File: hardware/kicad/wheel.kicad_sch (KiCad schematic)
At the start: 6 parts, among them J401 Deutsch DTM 3p (sensore), U401 EL817

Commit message: Translate code, hardware and docs to English; bilingual dashboard
- tdm-logic i18n module: every dashboard text in English and Italian,
  chosen by `[display] language` in the profile (English by default, the
  TDM 850 profile keeps Italian); number formatting per language
- Slint fixed labels moved to a `Labels` global filled from the same table;
  `tdm-dash --language en|it`; reference screens regenerated in English with
  Italian check screens
- tdmctl, tdm-dash CLI, simulator scenarios, calibration errors and tools
  print English
- KiCad sheets, WireViz harnesses, perfboard plan and CAD comments in
  English, exports regenerated with the new names
- manual, research, ADRs and READMEs translated; files renamed (docs/manual,
  docs/research, English chapter and ADR names); status markers are now
  [VERIFIED] / [TO VERIFY] / [HYPOTHESIS]

Co-Authored-By: Claude Opus 5.5 <noreply@anthropic.com>
Claude-Session: https://claude.ai/code/session_01G9D4Wshjz9MkaThp4wsrGP
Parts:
- J401: value Deutsch DTM 3p (sensore) -> Deutsch DTM 3p (sensor)
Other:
- note added: "LJ12A3-4-Z/BX inductive NPN normally open: in front of a bolt the output goes to ground. +12V_P → 2.2 kΩ → EL817 LED → sensor output. External 4.7 kΩ pull-up for fast edges. Sensor colours: brown +12 V, blue ground, black signal."
- note added: "Speed sensor"
- note added: "WHEEL → GP2, active low"
- note removed: "LJ12A3-4-Z/BX induttivo NPN normalmente aperto: davanti a un bullone l'uscita va a massa. +12V_P → 2,2 kΩ → LED dell'EL817 → uscita del sensore. Pull-up esterno da 4,7 kΩ per fronti veloci. Colori del sensore: marrone +12 V, blu massa, nero segnale."
- note removed: "Sensore di velocità"
- note removed: "WHEEL → GP2, attivo basso"
- title: Sensore ruota (LJ12A3) -> Wheel sensor (LJ12A3)
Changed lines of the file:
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@@
 	(paper "A4")
 	(title_block
-		(title "Sensore ruota (LJ12A3)")
+		(title "Wheel sensor (LJ12A3)")
 		(date "2026-10-21")
 		(rev "0.1")
 		(company "tdm-dash · CERN-OHL-P-2.0")
-		(comment 1 "Foglio 4 di 8")
-		(comment 2 "Generato da hardware/kicad/generate.py: non modificare a mano")
+		(comment 1 "Sheet 4 of 8")
+		(comment 2 "Generated by hardware/kicad/generate.py: do not edit by hand")
 	)
 	(symbol
@@
 			)
 		)
-		(property "Value" "Deutsch DTM 3p (sensore)"
+		(property "Value" "Deutsch DTM 3p (sensor)"
 			(at 30.48 71.12 0)
 			(effects
@@
 		)
 	)
-	(text "Sensore di velocità"
+	(text "Speed sensor"
 		(exclude_from_sim no)
 		(at 10.16 12.7 0)
@@
 		)
 	)
-	(text "LJ12A3-4-Z/BX induttivo NPN normalmente aperto: davanti a un bullone l'uscita va a massa.\n+12V_P → 2,2 kΩ → LED dell'EL817 → uscita del sensore. Pull-up esterno da 4,7 kΩ per fronti veloci.\nColori del sensore: marrone +12 V, blu massa, nero segnale."
+	(text "LJ12A3-4-Z/BX inductive NPN normally open: in front of a bolt the output goes to ground.\n+12V_P → 2.2 kΩ → EL817 LED → sensor output. External 4.7 kΩ pull-up for fast edges.\nSensor colours: brown +12 V, blue ground, black signal."
 		(exclude_from_sim no)
 		(at 10.16 17.78 0)
@@
 		)
 	)
-	(text "WHEEL → GP2, attivo basso"
+	(text "WHEEL → GP2, active low"
 		(exclude_from_sim no)
 		(at 167.64 81.28 0)

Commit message: English README, ADR 0012, CLAUDE.md rules, banner; consistent spelling
- README and docs/assets in English, banner tagline "Open-source digital
  instrument cluster" and regenerated banner
- ADR 0012: English repository, bilingual dashboard
- CLAUDE.md: English everywhere, dashboard texts in both languages through
  tdm-logic i18n, new status markers
- American spelling across docs, harness labels and schematic notes;
  ADR 0007 renamed to 0007-licenses; exports and screens regenerated

Co-Authored-By: Claude Opus 5.5 <noreply@anthropic.com>
Claude-Session: https://claude.ai/code/session_01G9D4Wshjz9MkaThp4wsrGP
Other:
- note added: "LJ12A3-4-Z/BX inductive NPN normally open: in front of a bolt the output goes to ground. +12V_P → 2.2 kΩ → EL817 LED → sensor output. External 4.7 kΩ pull-up for fast edges. Sensor colors: brown +12 V, blue ground, black signal."
- note removed: "LJ12A3-4-Z/BX inductive NPN normally open: in front of a bolt the output goes to ground. +12V_P → 2.2 kΩ → EL817 LED → sensor output. External 4.7 kΩ pull-up for fast edges. Sensor colours: brown +12 V, blue ground, black signal."
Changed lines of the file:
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@@
 		)
 	)
-	(text "LJ12A3-4-Z/BX inductive NPN normally open: in front of a bolt the output goes to ground.\n+12V_P → 2.2 kΩ → EL817 LED → sensor output. External 4.7 kΩ pull-up for fast edges.\nSensor colours: brown +12 V, blue ground, black signal."
+	(text "LJ12A3-4-Z/BX inductive NPN normally open: in front of a bolt the output goes to ground.\n+12V_P → 2.2 kΩ → EL817 LED → sensor output. External 4.7 kΩ pull-up for fast edges.\nSensor colors: brown +12 V, blue ground, black signal."
 		(exclude_from_sim no)
 		(at 10.16 17.78 0)

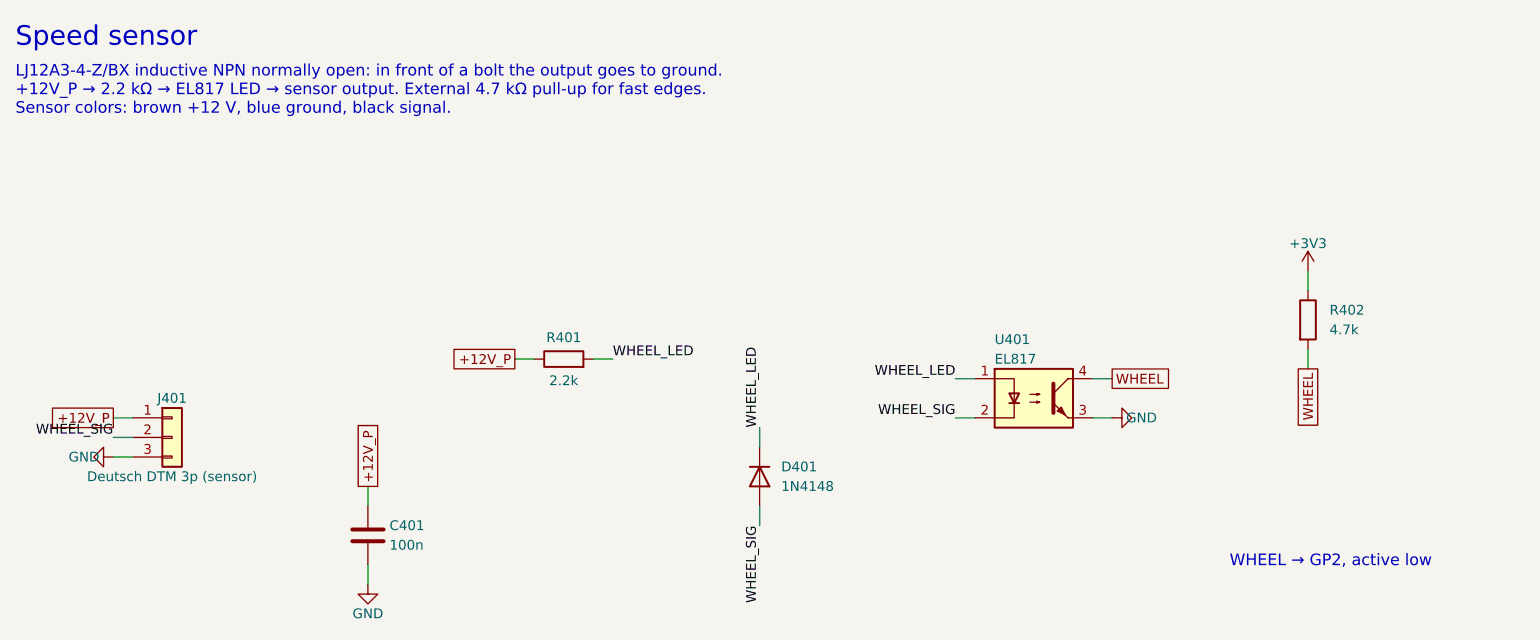
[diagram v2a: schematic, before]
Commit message: Schematic: drawn wires, block diagram, new title block
The sheets were a netlist in disguise: every pin ended in a short stub and
a label, so the circuits had to be pieced together by name, labels
overlapped, two sheets fell off the index page and the title block was
KiCad's default. The generator now draws the schematic:

- hardware/kicad/schgen: placement on the 50 mil grid, orthogonal wires,
  junctions, hierarchical ports, module and connector symbols with named
  pins; the drawing is normalised the way KiCad 9 reads it and checked
  against the declared netlist (no wire may connect anything else)
- hardware/kicad/sheets: one module per sheet, laid out left to right
  from the bike to the Pico; the root sheet is a block diagram whose
  wires are the signals between sheets
- tdm-dash.kicad_wks: frame and title block of the project
- symbols copied from KiCad 9.0.9 (vendor_symbols.py): the generator no
  longer needs KiCad installed
- export.sh: ERC, tools/check_netlist.py (KiCad's netlist is the declared
  one), check_pinmap.py, PDF and SVG on white, tools/check_svg_layout.py
  (no text over another text, a wire, the frame or the title block)

The circuit is unchanged: KiCad's netlist of the old and new schematic
has the same 56 nets (FRAM pins now follow the breakout header, R603/R604
pins swapped).

Co-Authored-By: Claude Opus 5.5 <noreply@anthropic.com>
Claude-Session: https://claude.ai/code/session_01G9D4Wshjz9MkaThp4wsrGP
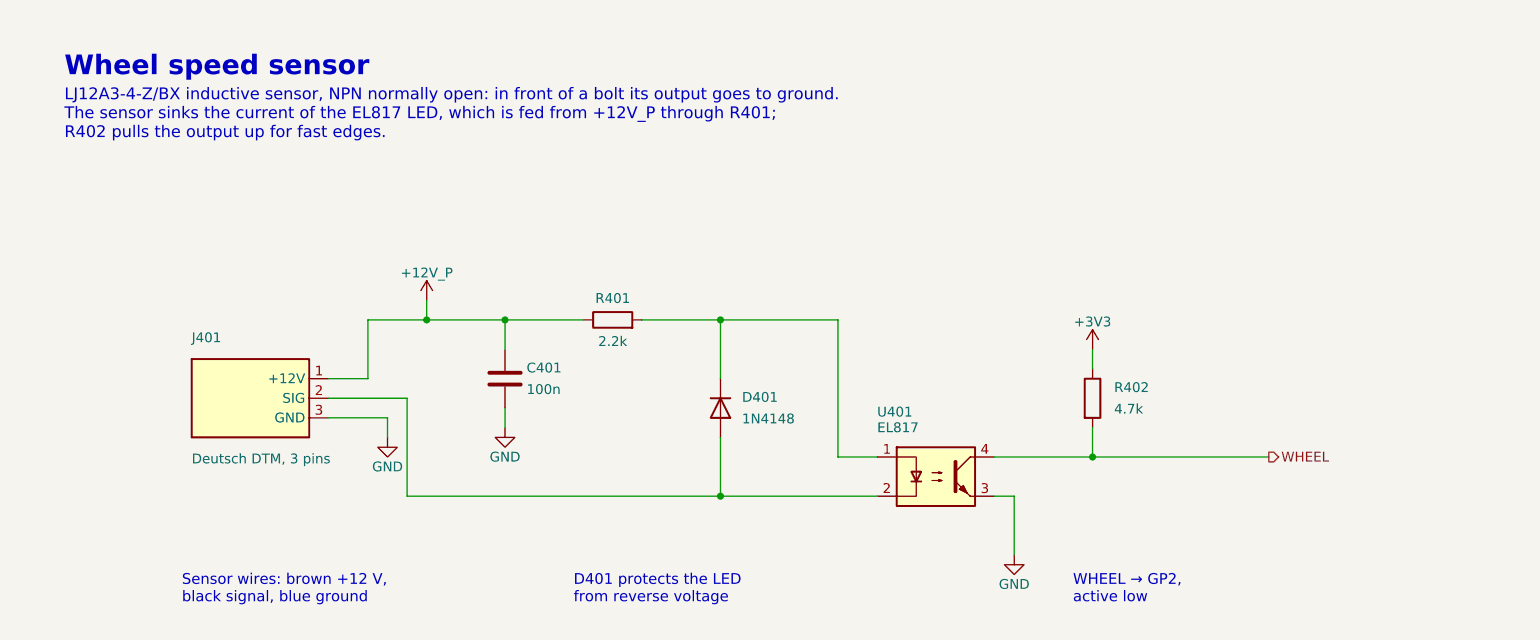
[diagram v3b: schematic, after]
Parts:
- removed J401: Deutsch DTM 3p (sensor), symbol Connector_Generic:Conn_01x03
- added J401: Deutsch DTM, 3 pins, symbol tdm:Conn_Sensor3
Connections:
- net +12V_P: now also J401.1 (+12V)
- net GND: now also J401.3 (GND)
- net WHEEL_LED: no longer names the net of D401.1 (K), R401.2, U401.1
- net WHEEL_SIG: no longer names the net of D401.2 (A), U401.2
- net WHEEL_SIG: now also J401.2 (SIG)
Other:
- note added: "D401 protects the LED from reverse voltage"
- note added: "LJ12A3-4-Z/BX inductive sensor, NPN normally open: in front of a bolt its output goes to ground. The sensor sinks the current of the EL817 LED, which is fed from +12V_P through R401; R402 pulls the output up for fast edges."
- note added: "Sensor wires: brown +12 V, black signal, blue ground"
- note added: "Wheel speed sensor"
- note removed: "LJ12A3-4-Z/BX inductive NPN normally open: in front of a bolt the output goes to ground. +12V_P → 2.2 kΩ → EL817 LED → sensor output. External 4.7 kΩ pull-up for fast edges. Sensor colors: brown +12 V, blue ground, black signal."
- note removed: "Speed sensor"
- company: tdm-dash · CERN-OHL-P-2.0 -> tdm-dash

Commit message: Schematic: backlight breakout off the board, harness fuse, micro-USB plug
The perfboard has no room for the TPS61169 breakout, and the build steps
already wired it off the board: J701 now gives it +5 V, CTRL and ground,
and its output goes to the panel LED pins (J704), in a dashed box like the
buttons. F101 is marked as the inline fuse of the adapter harness, J401 as
the terminal for the sensor cable, and J703 has the five pins of the
micro-USB plug, with ID tied to ground.

Co-Authored-By: Claude Opus 5.5 <noreply@anthropic.com>
Claude-Session: https://claude.ai/code/session_01G9D4Wshjz9MkaThp4wsrGP
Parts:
- J401: value Deutsch DTM, 3 pins -> to the wheel sensor
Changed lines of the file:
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@@
 			)
 		)
-		(property "Value" "Deutsch DTM, 3 pins"
+		(property "Value" "to the wheel sensor"
 			(at 33.02 68.072 0)
 			(effects
@@
 			)
 		)
-		(property "Description" "Wheel sensor connector"
+		(property "Description" "Wheel sensor cable, from the DTM connector at the fork"
 			(at 40.64 60.96 0)
 			(effects
